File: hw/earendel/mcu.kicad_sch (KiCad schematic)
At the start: 16 parts, among them SW1 SW_Push, U1 RP2040

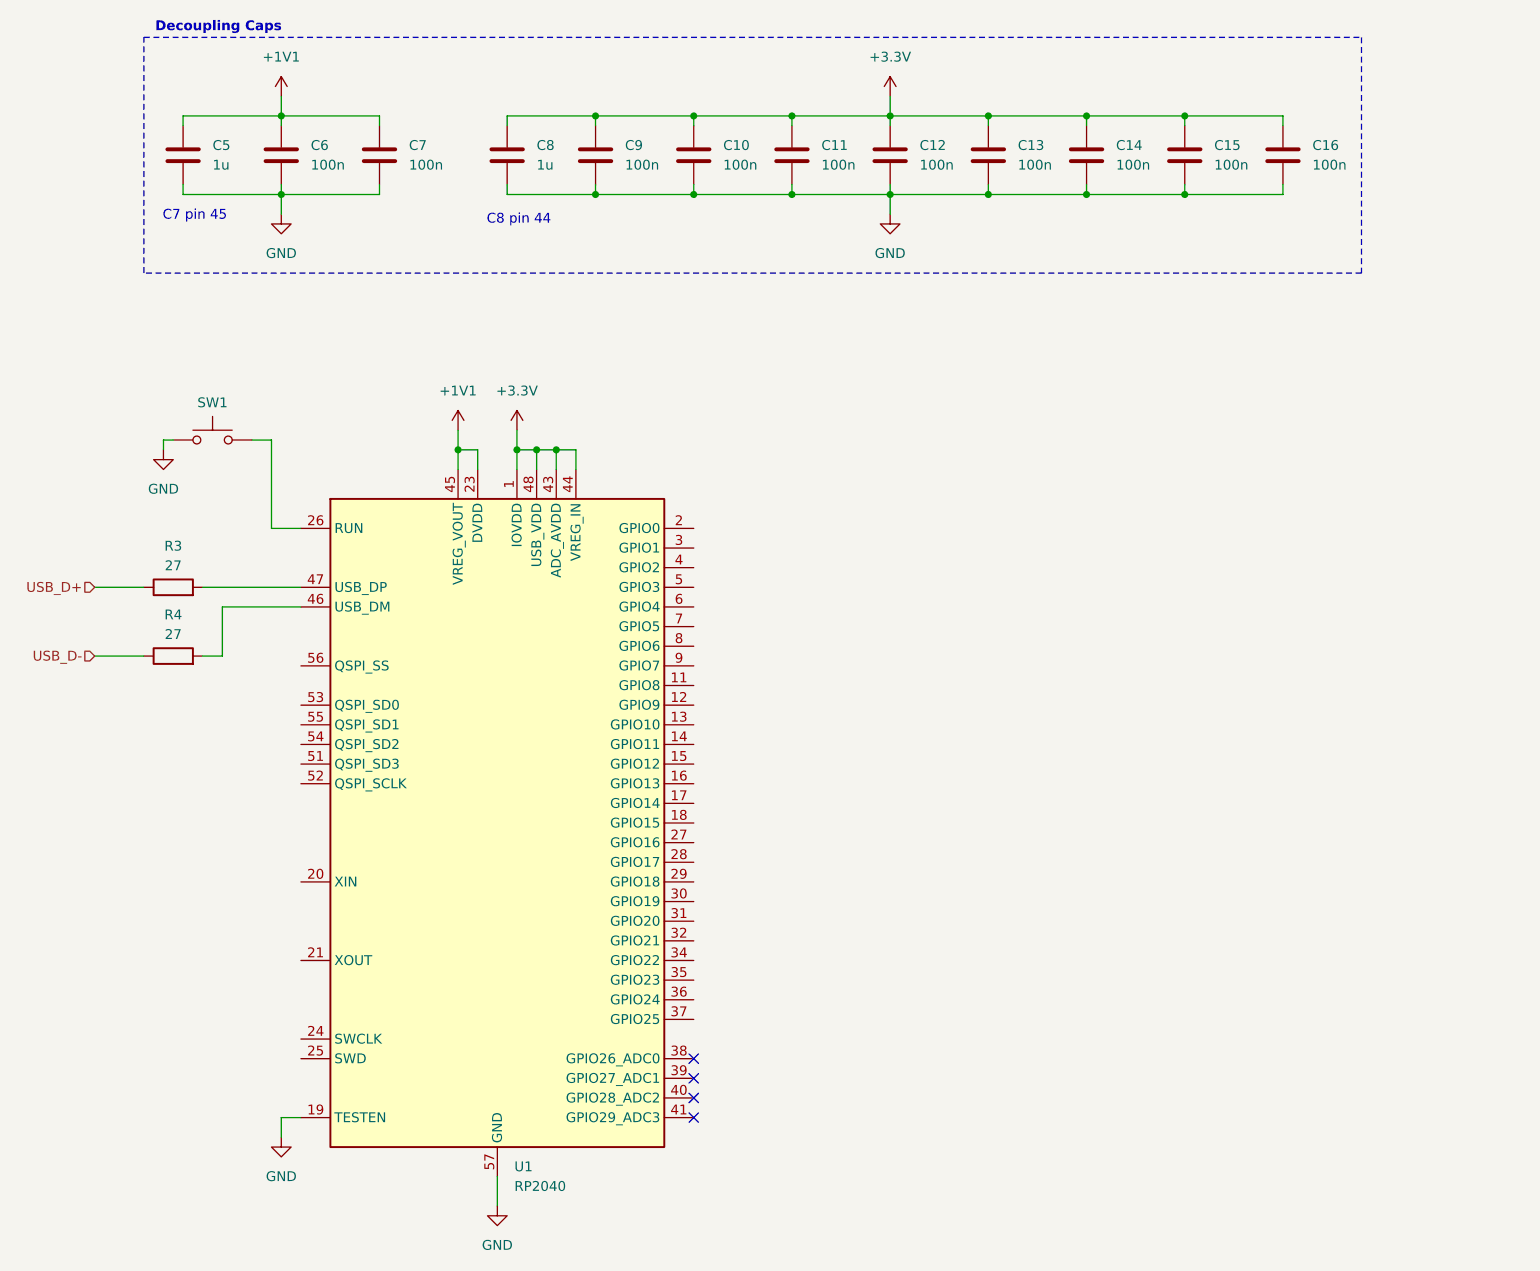
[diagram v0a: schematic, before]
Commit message: New blank kicad project, add esp32 mcu and initial usb connector
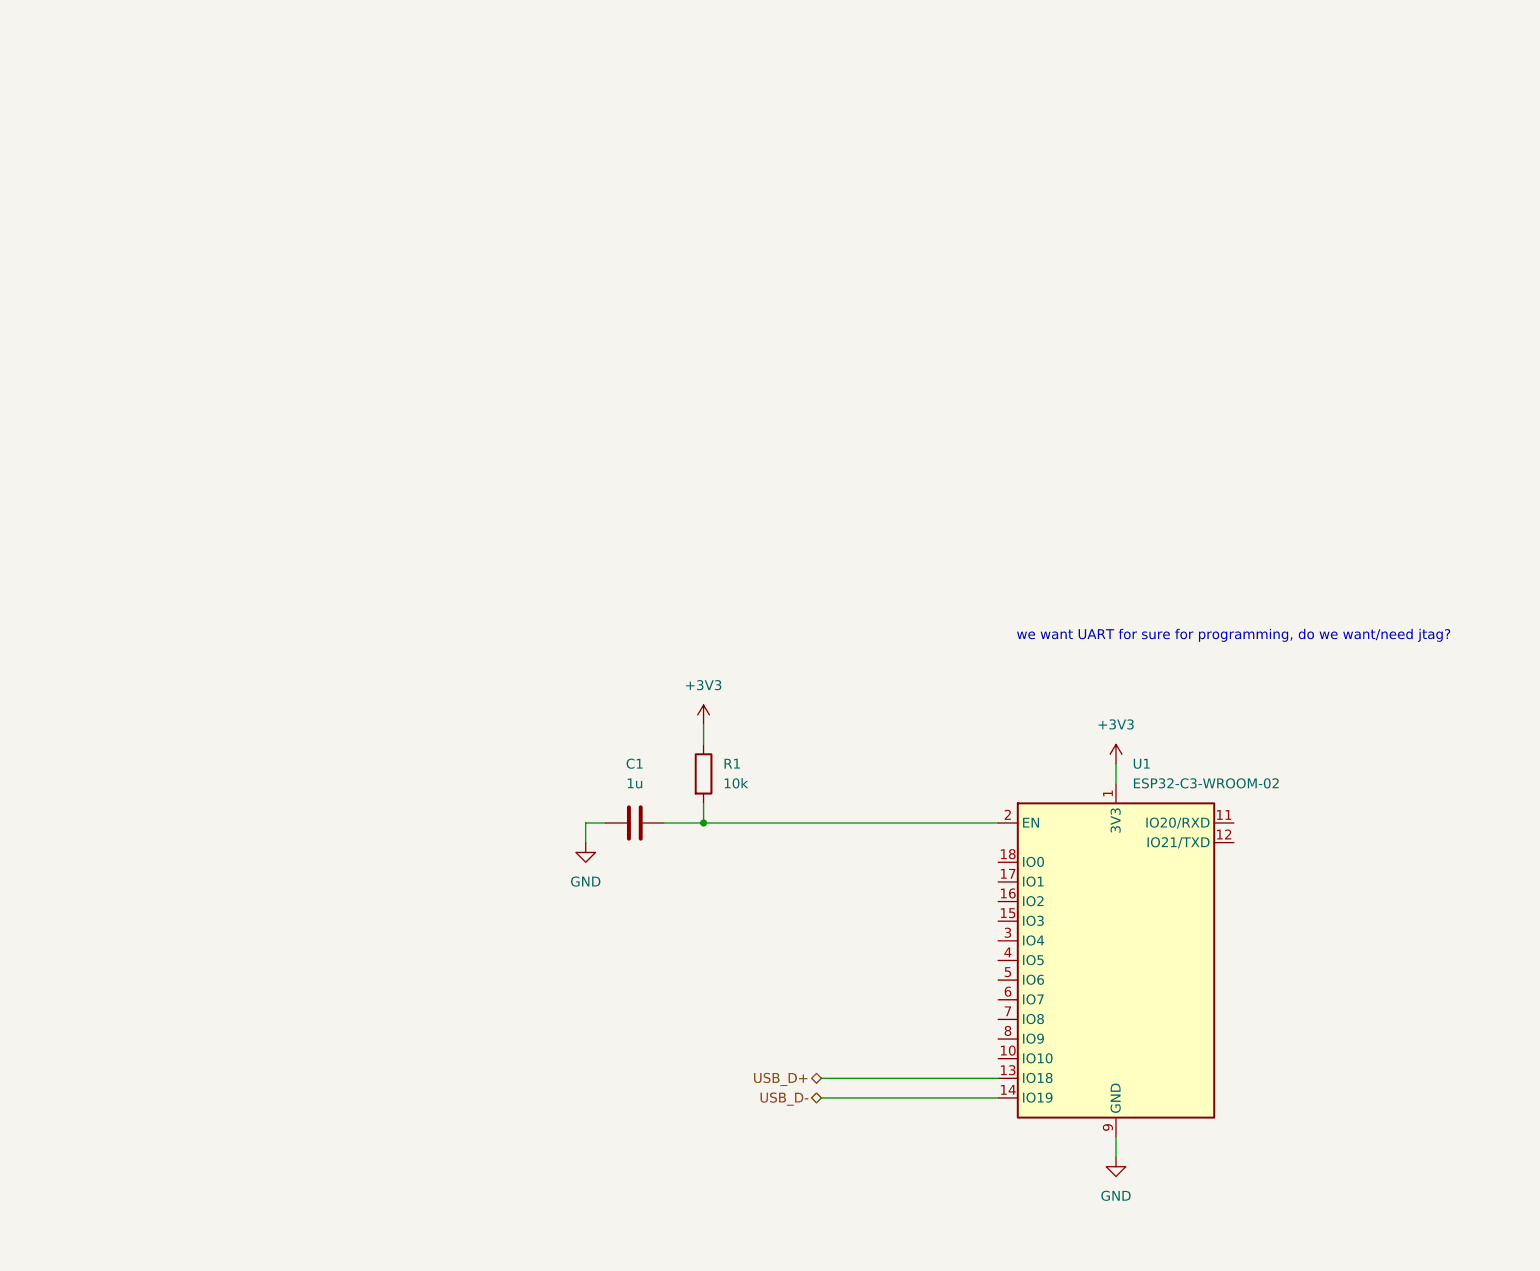
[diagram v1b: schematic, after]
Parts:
- removed C10, C11, C12, C13, C14, C15, C16, C6, C7, C9: 100n, symbol Device:C
- removed C5, C8: 1u, symbol Device:C
- removed R3, R4: 27, symbol Device:R
- removed SW1: SW_Push, symbol Switch:SW_Push
- removed U1: RP2040, Package_DFN_QFN:QFN-56-1EP_7x7mm_P0.4mm_EP3.2x3.2mm, symbol MCU_RaspberryPi:RP2040
- added C1: 1u, Capacitor_SMD:C_0603_1608Metric, symbol Device:C
- added R1: 10k, Resistor_SMD:R_0603_1608Metric, symbol Device:R
- added U1: ESP32-C3-WROOM-02, RF_Module:ESP32-C3-WROOM-02, symbol RF_Module:ESP32-C3-WROOM-02
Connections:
- net GND: now also C1.1, U1.19 (GND), U1.9 (GND)
- net USB_D+: now also U1.13 (IO18)
- net USB_D-: now also U1.14 (IO19)
- new net: C1.2, R1.2, U1.2 (EN)
- new net +3V3: R1.1, U1.1 (3V3)
- no-connect marks 4 -> 0
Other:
- note added: "we want UART for sure for programming, do we want/need jtag?"
- note removed: "C7 pin 45"
- note removed: "C8 pin 44"
- note removed: "Decoupling Caps"
- company: Aaron & Ryan Shappell -> Catlock
- title: (none) -> Earendel Microscope Ring Light
